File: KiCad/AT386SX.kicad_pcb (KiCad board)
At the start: 2 copper layers, 172.7 x 218.4 mm, 160 parts, among them J1 BANK0, J10 BUSAT_HOST, J11 PS/2 Dual Port, J12 Power, J13 Front Panel, J14 CPU 1-25, J15 CPU 26-50, J16 CPU 51-75, J17 CPU 76-100, J2 BANK0, J3 BANK1, J4 BANK1, J5 BUSAT_HOST, J6 BUSAT_HOST, J7 BUSAT_HOST, J8 BUSAT_HOST, J9 BUSAT_HOST, Q1 2N3904, SW1 Power, SW2 Reset, U1 80386SX, U10 LM7905, U2 80387SX, U3 RC2016A5, U4 DS12885, U5 8242KBD, U6 SST39SF010A, U7 74HC05, U8 74HCT14, U9 74HCT74, X1 CPU_CLK, X2 FPU_CLK, Y1 14.31818MHz, Y2 32768Hz

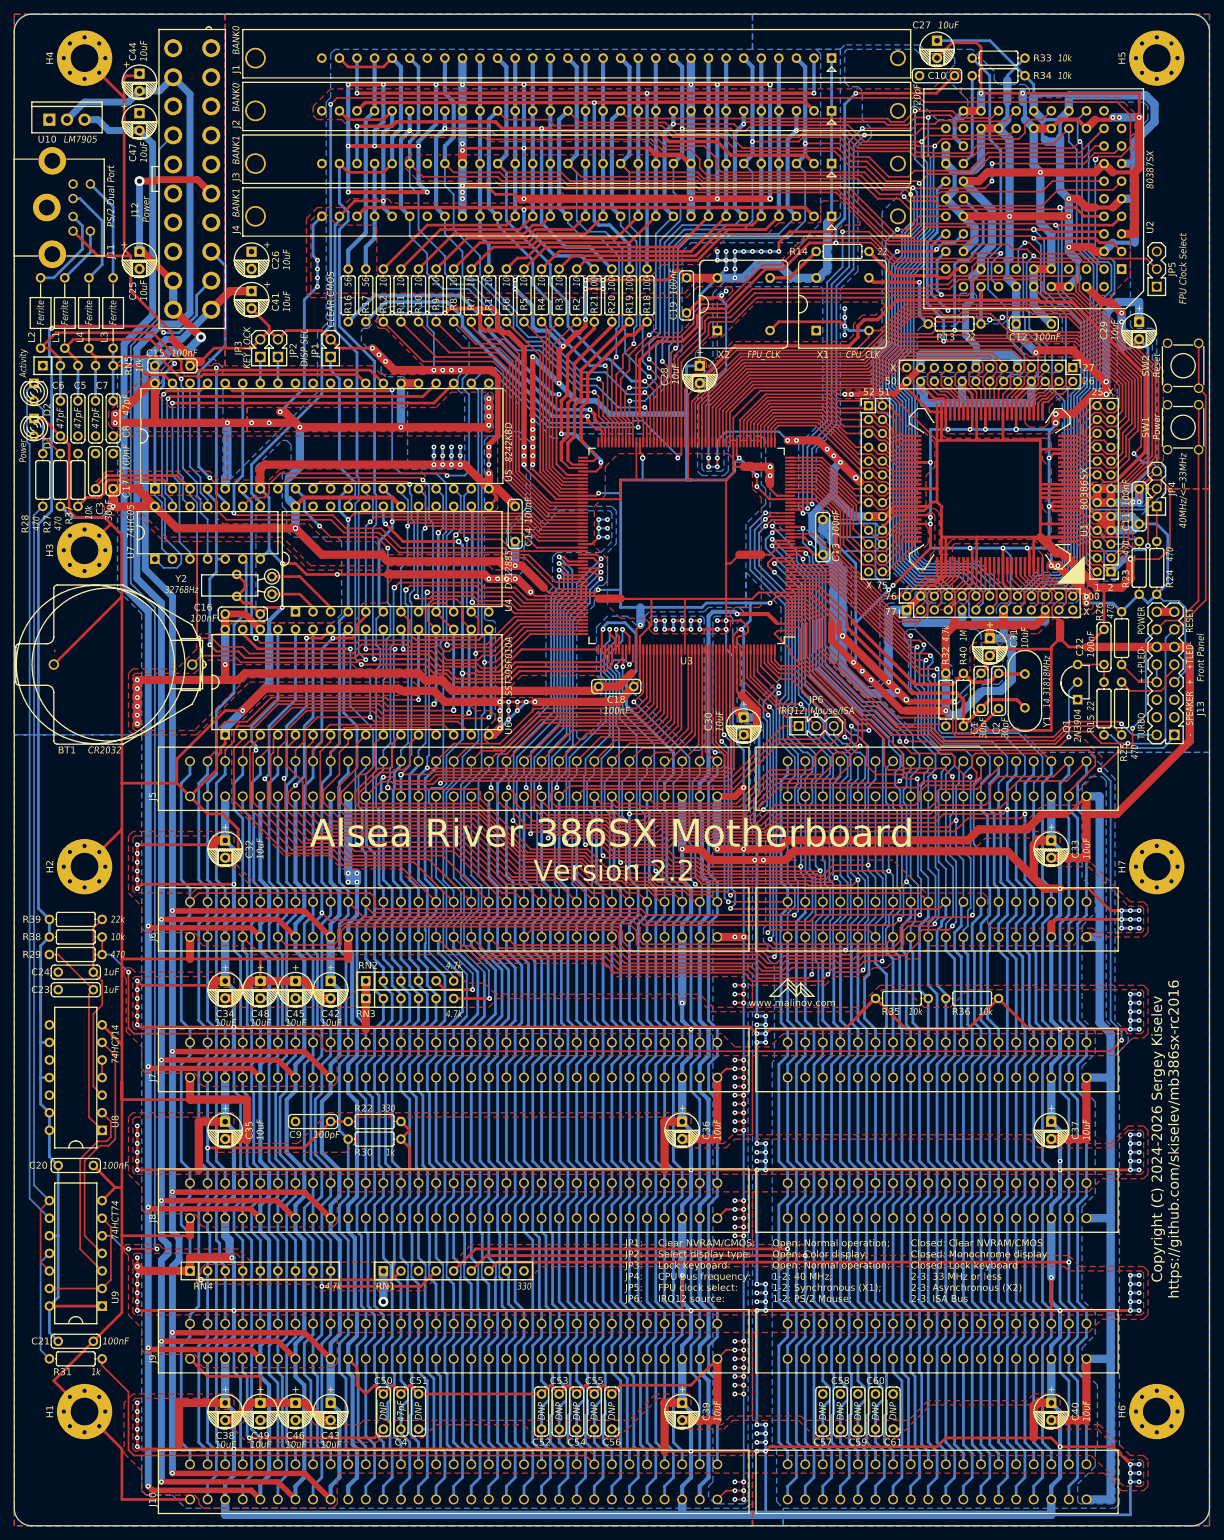
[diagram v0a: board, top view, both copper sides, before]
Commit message: Add a polyfuse for the PS/2 port
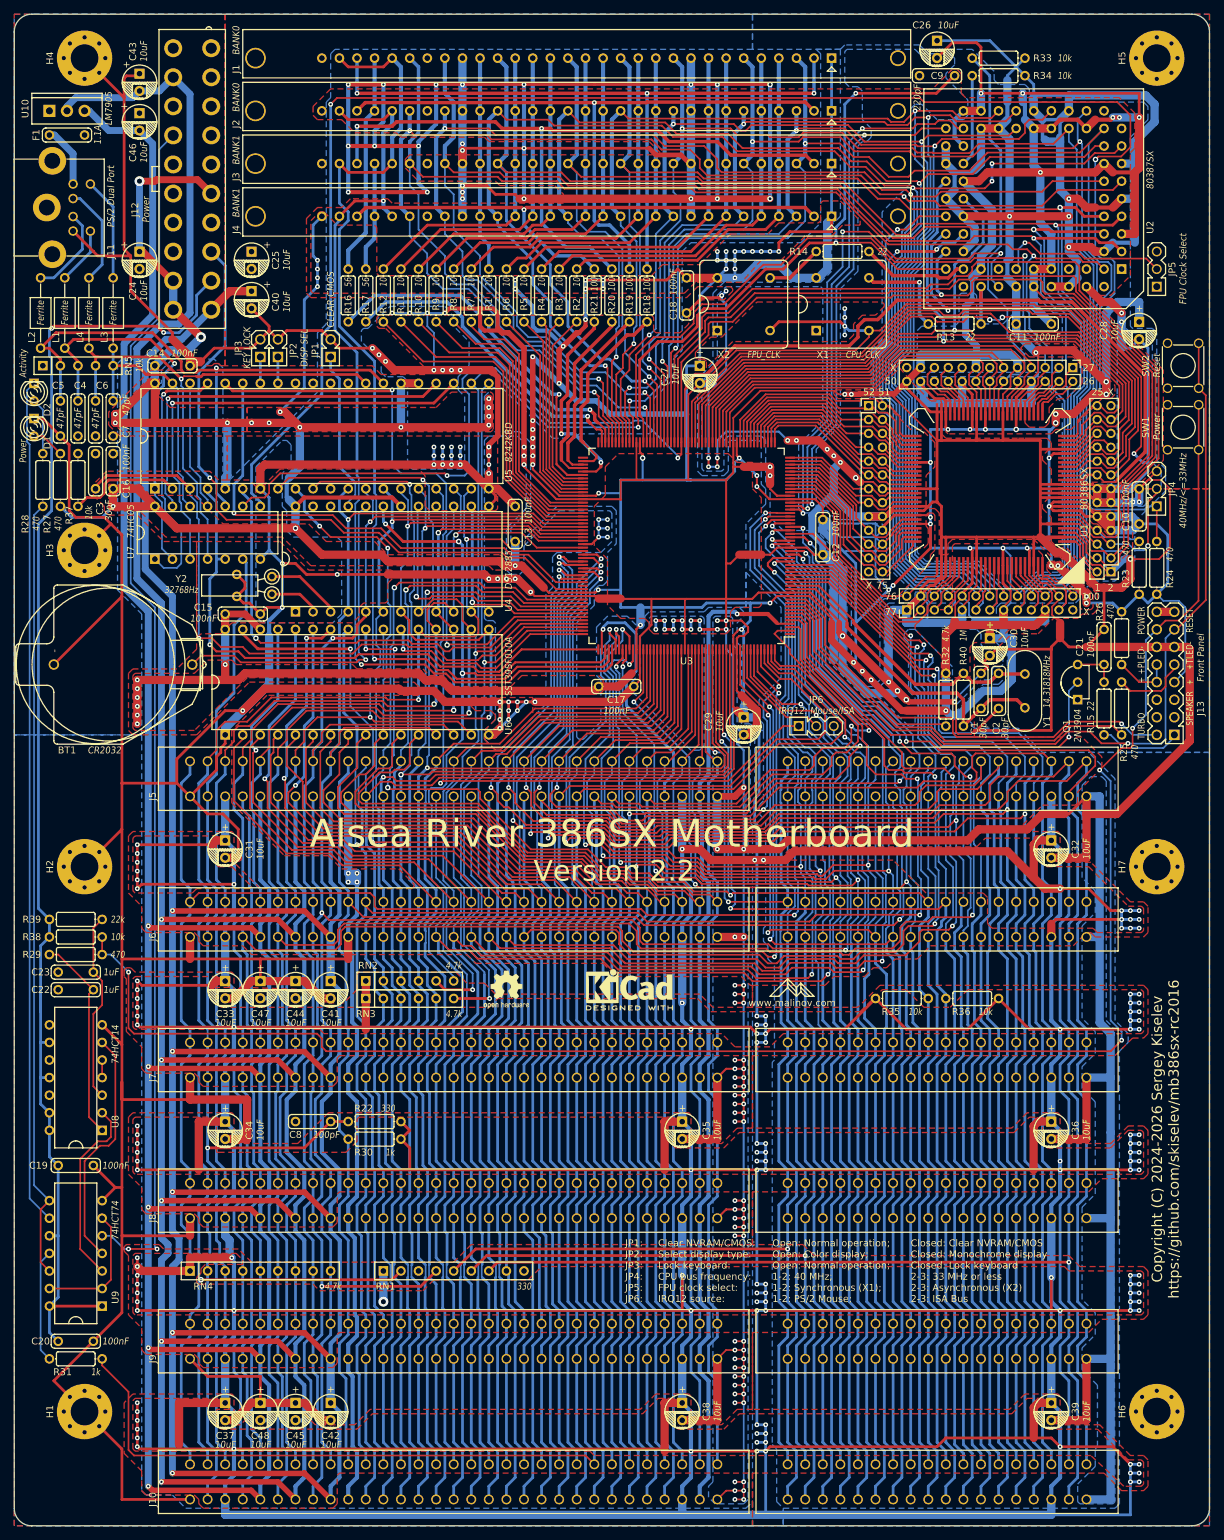
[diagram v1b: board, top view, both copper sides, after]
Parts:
- removed the C4 at (73.7, 219.7)
- removed C50, C51, C52, C53, C54, C55, C56, C57, C58, C59, C60, C61: DNP, My_Components:Cap_Cer_508
- added F1: 1.1A, My_Components:Cap_Cer_508, F.Cu at (25.4, 35.2)
- added LOGO1: Logo_Open_Hardware_Small, Symbol:OSHW-Logo2_7.3x6mm_SilkScreen, F.Cu at (88.9, 158.8)
- added LOGO2: Logo_Open_Hardware_Small, Symbol:KiCad-Logo2_5mm_SilkScreen, F.Cu at (106.7, 158.8)
- moved U10 1.27 mm to (25.4, 31.8)
- renumbered C11 to C10, C12 to C11, C13 to C12, C14 to C13, C15 to C14, C16 to C15, C17 to C16, C18 to C17, C19 to C18, C20 to C19, C21 to C20, C22 to C21, C23 to C22, C24 to C23, C25 to C24, C26 to C25, C27 to C26, C28 to C27, C29 to C28, C30 to C29, C31 to C30, C32 to C31, C33 to C32, C34 to C33, C35 to C34, C36 to C35, C37 to C36, C38 to C37, C39 to C38, C40 to C39, C5 to C4, C41 to C40, C42 to C41, C43 to C42, C44 to C43, C45 to C44, C46 to C45, C47 to C46, C48 to C47, C49 to C48, C6 to C5, C7 to C6, C8 to C7, C9 to C8, C10 to C9
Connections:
- net ~{MCAS0} renamed ~{CAS0}
- net ~{MCAS1} renamed ~{CAS1}
- net ~{MCAS2} renamed ~{CAS2}
- net ~{MCAS3} renamed ~{CAS3}
- net ~{MRAS01} renamed ~{RAS01}
- net ~{MRAS23} renamed ~{RAS23}
- J11 pad 4: VCC -> Net-(J11-Pad4)
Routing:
- net GND: track 3052.6 -> 2987.4 mm
- net IRQ9: track 255.5 -> 235.6 mm, vias 3 -> 2
- net VCC: track 3023.7 -> 3032.8 mm
- net Net-(J11-Pad4): track 0.00 -> 8.92 mm
- net IRQ3: track 168.7 -> 167.4 mm
- net IRQ14: track 170.3 -> 169.0 mm
- net ~{IOR}: track 238.8 -> 237.6 mm
- net IRQ6: track 166.5 -> 165.7 mm
- net IRQ12: track 120.7 -> 119.9 mm
- net IRQ10: track 135.3 -> 134.5 mm
- net IRQ4: track 172.7 -> 171.9 mm
- net IRQ11: track 137.7 -> 136.8 mm
- net ~{IOW}: track 235.0 -> 234.2 mm
- net IRQ7: track 168.2 -> 167.3 mm
- net IRQ5: track 167.5 -> 166.7 mm
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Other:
- board text added: "K_VCC"
- board text added: "~{CAS0}"
- board text added: "~{CAS1}"
- board text added: "~{CAS2}"
- board text added: "~{CAS3}"
- board text added: "~{RAS01}"
- board text added: "~{RAS23}"
- board text removed: "MDP02"
- board text removed: "MDP13"
- board text removed: "~{RCAS0}"
- board text removed: "~{RCAS1}"
- board text removed: "~{RCAS2}"
- board text removed: "~{RCAS3}"
- board text removed: "~{RRAS01}"
- board text removed: "~{RRAS23}"

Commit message: Add version 2.3 files
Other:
- board text added: "Acknowledgements: Marco Both (https://www.youtube.com/@Nelson68k): M396F motherboard replica: https://github.com/Marco-Both/M396F-Replika Maxim Nasonov: SARC RC2016 chipset reverse engineering and firmware Konstantinos Galanopoulos (https://www.youtube.com/@atheatos): 386SX socket idea, SARC RC2016 motherboards mods Alexander Jacocks, Mikhail Andreev - Early adpopters"
- board text added: "Alsea River 386SX Motherboard - Version 2.3 Copyright (C) 2024-2026 Sergey Kiselev https://github.com/skiselev/mb386sx-rc2016"
- board text added: "Version 2.3"
- board text removed: "Alsea River 386SX Motherboard - Version 2.2 Copyright (C) 2024-2026 Sergey Kiselev https://github.com/skiselev/mb386sx-rc2016 Based on the M396F motherboard replica by Marco Both: https://github.com/skiselev/mb386sx-rc2016"
- board text removed: "Copyright (C) 2024-2026 Sergey Kiselev https://github.com/skiselev/mb386sx-rc2016"
- board text removed: "Version 2.2"
